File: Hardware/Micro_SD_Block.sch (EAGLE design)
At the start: 14 parts, among them U1 USD-SOCKETNEW, U2 EDISON_CONNECTOR_FULLMOUNTING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, U3 EDISON_CONNECTOR_FULLHEADER

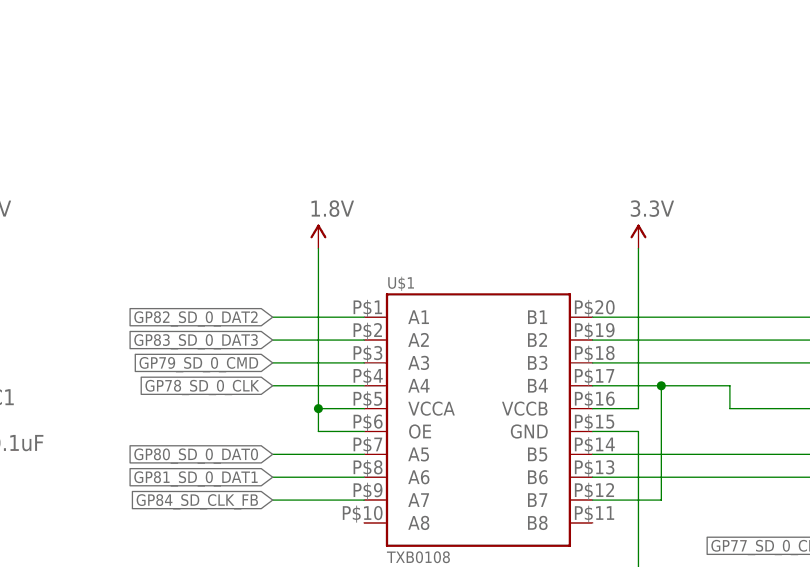
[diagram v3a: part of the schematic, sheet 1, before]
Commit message: Ready for reds Struck one weird leftover via Renamed TXB0108 chip refdes To-do: fix the TXB0108 symbol to remove P$ from pin names. Do in library and update to design!
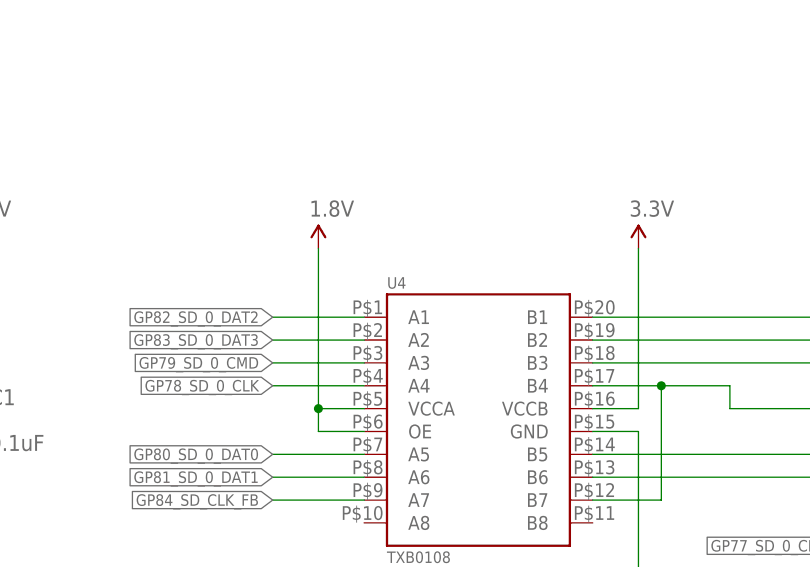
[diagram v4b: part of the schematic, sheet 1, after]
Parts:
- renumbered U$1 to U4
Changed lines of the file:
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@@
 <layer number="255" name="routoute" color="7" fill="1" visible="yes" active="yes"/>
 </layers>
-<schematic xreflabel="%F%N/%S" xrefpart="1_/%S.%C%R">
+<schematic xreflabel="%F%N/%S" xrefpart="/%S.%C%R">
 <attributes>
 </attributes>
@@
 <part name="FID3" library="SparkFun-Aesthetics" deviceset="FIDUCIAL" device="1X2"/>
 <part name="FID4" library="SparkFun-Aesthetics" deviceset="FIDUCIAL" device="1X2"/>
-<part name="U$1" library="Testing" deviceset="TXB0108" device=""/>
+<part name="U4" library="Testing" deviceset="TXB0108" device=""/>
 <part name="GND2" library="SparkFun-Aesthetics" deviceset="GND" device=""/>
 <part name="SUPPLY1" library="SparkFun-Aesthetics" deviceset="3.3V" device=""/>
@@
 <instance part="FID3" gate="G$1" x="246.38" y="30.48"/>
 <instance part="FID4" gate="G$1" x="241.3" y="30.48"/>
-<instance part="U$1" gate="G$1" x="121.92" y="109.22"/>
+<instance part="U4" gate="G$1" x="121.92" y="109.22"/>
 <instance part="GND2" gate="1" x="132.08" y="83.82"/>
 <instance part="SUPPLY1" gate="G$1" x="132.08" y="127"/>
@@
 </segment>
 <segment>
-<pinref part="U$1" gate="G$1" pin="GND"/>
+<pinref part="U4" gate="G$1" pin="GND"/>
 <wire x1="127" y1="106.68" x2="132.08" y2="106.68" width="0.1524" layer="91"/>
 <wire x1="132.08" y1="106.68" x2="132.08" y2="86.36" width="0.1524" layer="91"/>
@@
 <wire x1="101.6" y1="111.76" x2="91.44" y2="111.76" width="0.1524" layer="91"/>
 <label x="91.44" y="111.76" size="1.27" layer="95" rot="R180" xref="yes"/>
-<pinref part="U$1" gate="G$1" pin="A4"/>
+<pinref part="U4" gate="G$1" pin="A4"/>
 </segment>
 </net>
@@
 <wire x1="101.6" y1="114.3" x2="91.44" y2="114.3" width="0.1524" layer="91"/>
 <label x="91.44" y="114.3" size="1.27" layer="95" rot="R180" xref="yes"/>
-<pinref part="U$1" gate="G$1" pin="A3"/>
+<pinref part="U4" gate="G$1" pin="A3"/>
 </segment>
 </net>
@@
 <wire x1="101.6" y1="104.14" x2="91.44" y2="104.14" width="0.1524" layer="91"/>
 <label x="91.44" y="104.14" size="1.27" layer="95" rot="R180" xref="yes"/>
-<pinref part="U$1" gate="G$1" pin="A5"/>
+<pinref part="U4" gate="G$1" pin="A5"/>
 </segment>
 </net>
@@
 <wire x1="101.6" y1="101.6" x2="91.44" y2="101.6" width="0.1524" layer="91"/>
 <label x="91.44" y="101.6" size="1.27" layer="95" rot="R180" xref="yes"/>
-<pinref part="U$1" gate="G$1" pin="A6"/>
+<pinref part="U4" gate="G$1" pin="A6"/>
 </segment>
 </net>
@@
 <wire x1="101.6" y1="119.38" x2="91.44" y2="119.38" width="0.1524" layer="91"/>
 <label x="91.44" y="119.38" size="1.27" layer="95" rot="R180" xref="yes"/>
-<pinref part="U$1" gate="G$1" pin="A1"/>
+<pinref part="U4" gate="G$1" pin="A1"/>
 </segment>
 </net>
@@
 <wire x1="101.6" y1="116.84" x2="91.44" y2="116.84" width="0.1524" layer="91"/>
 <label x="91.44" y="116.84" size="1.27" layer="95" rot="R180" xref="yes"/>
-<pinref part="U$1" gate="G$1" pin="A2"/>
+<pinref part="U4" gate="G$1" pin="A2"/>
 </segment>
 </net>
 <net name="N$1" class="0">
 <segment>
-<pinref part="U$1" gate="G$1" pin="B1"/>
+<pinref part="U4" gate="G$1" pin="B1"/>
 <pinref part="U1" gate="G$1" pin="NC"/>
 <wire x1="127" y1="119.38" x2="162.56" y2="119.38" width="0.1524" layer="91"/>
@@
 <segment>
 <pinref part="U1" gate="G$1" pin="CS"/>
-<pinref part="U$1" gate="G$1" pin="B2"/>
+<pinref part="U4" gate="G$1" pin="B2"/>
 <wire x1="162.56" y1="116.84" x2="127" y2="116.84" width="0.1524" layer="91"/>
 </segment>
@@
 <net name="N$3" class="0">
 <segment>
-<pinref part="U$1" gate="G$1" pin="B3"/>
+<pinref part="U4" gate="G$1" pin="B3"/>
 <pinref part="U1" gate="G$1" pin="DI"/>
 <wire x1="127" y1="114.3" x2="162.56" y2="114.3" width="0.1524" layer="91"/>
@@
 <net name="SCK" class="0">
 <segment>
-<pinref part="U$1" gate="G$1" pin="B4"/>
+<pinref part="U4" gate="G$1" pin="B4"/>
 <wire x1="127" y1="111.76" x2="134.62" y2="111.76" width="0.1524" layer="91"/>
 <wire x1="134.62" y1="111.76" x2="142.24" y2="111.76" width="0.1524" layer="91"/>
@@
 <pinref part="U1" gate="G$1" pin="SCK"/>
 <wire x1="142.24" y1="109.22" x2="162.56" y2="109.22" width="0.1524" layer="91"/>
-<pinref part="U$1" gate="G$1" pin="B7"/>
+<pinref part="U4" gate="G$1" pin="B7"/>
 <wire x1="127" y1="99.06" x2="134.62" y2="99.06" width="0.1524" layer="91"/>
 <wire x1="134.62" y1="99.06" x2="134.62" y2="111.76" width="0.1524" layer="91"/>
@@
 <net name="N$5" class="0">
 <segment>
-<pinref part="U$1" gate="G$1" pin="B5"/>
+<pinref part="U4" gate="G$1" pin="B5"/>
 <pinref part="U1" gate="G$1" pin="DO"/>
 <wire x1="127" y1="104.14" x2="162.56" y2="104.14" width="0.1524" layer="91"/>
@@
 <net name="N$6" class="0">
 <segment>
-<pinref part="U$1" gate="G$1" pin="B6"/>
+<pinref part="U4" gate="G$1" pin="B6"/>
 <pinref part="U1" gate="G$1" pin="RSV"/>
 <wire x1="127" y1="101.6" x2="162.56" y2="101.6" width="0.1524" layer="91"/>
@@
 <net name="3.3V" class="0">
 <segment>
-<pinref part="U$1" gate="G$1" pin="VCCB"/>
+<pinref part="U4" gate="G$1" pin="VCCB"/>
 <wire x1="127" y1="109.22" x2="132.08" y2="109.22" width="0.1524" layer="91"/>
 <wire x1="132.08" y1="109.22" x2="132.08" y2="127" width="0.1524" layer="91"/>
@@
 <net name="1.8V" class="0">
 <segment>
-<pinref part="U$1" gate="G$1" pin="VCCA"/>
+<pinref part="U4" gate="G$1" pin="VCCA"/>
 <pinref part="SUPPLY3" gate="G$1" pin="1.8V"/>
 <wire x1="101.6" y1="109.22" x2="96.52" y2="109.22" width="0.1524" layer="91"/>
 <wire x1="96.52" y1="109.22" x2="96.52" y2="127" width="0.1524" layer="91"/>
-<pinref part="U$1" gate="G$1" pin="OE"/>
+<pinref part="U4" gate="G$1" pin="OE"/>
 <wire x1="101.6" y1="106.68" x2="96.52" y2="106.68" width="0.1524" layer="91"/>
 <wire x1="96.52" y1="106.68" x2="96.52" y2="109.22" width="0.1524" layer="91"/>
@@
 <wire x1="101.6" y1="99.06" x2="91.44" y2="99.06" width="0.1524" layer="91"/>
 <label x="91.44" y="99.06" size="1.27" layer="95" rot="R180" xref="yes"/>
-<pinref part="U$1" gate="G$1" pin="A7"/>
-</segment>
-</net>
+<pinref part="U4" gate="G$1" pin="A7"/>
+</segment>
+</net>

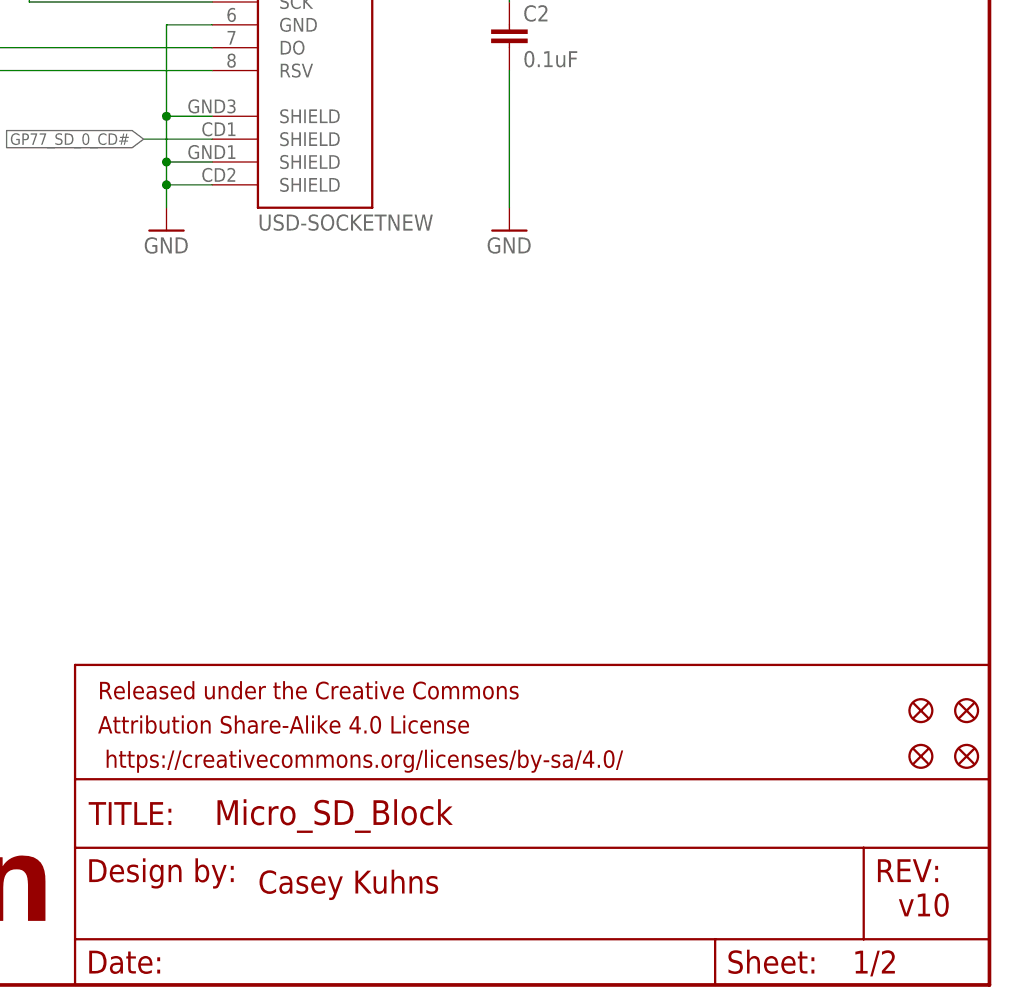
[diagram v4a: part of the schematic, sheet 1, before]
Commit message: fixed CD grounding issue, CD1 and CD2 are connected internally.
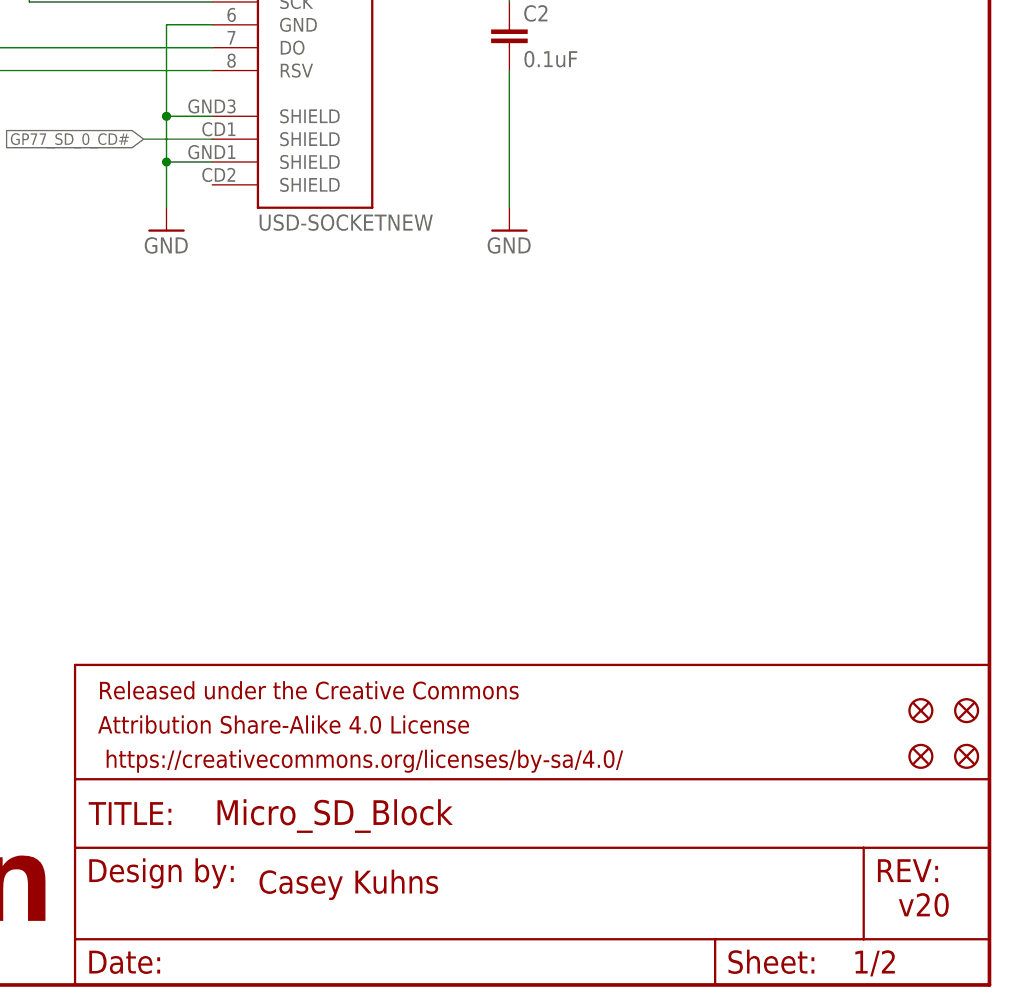
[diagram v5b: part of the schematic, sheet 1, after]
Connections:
- net GND: no longer U1.SHIELD@4
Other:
- note added: "v20"
- note removed: "v10"
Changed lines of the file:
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@@
 <?xml version="1.0" encoding="utf-8"?>
 <!DOCTYPE eagle SYSTEM "eagle.dtd">
-<eagle version="6.6.0">
+<eagle version="6.5.0">
 <drawing>
 <settings>
@@
 <plain>
 <text x="167.64" y="10.16" size="2.54" layer="94">Casey Kuhns</text>
-<text x="238.76" y="7.62" size="2.54" layer="94">v10</text>
+<text x="238.76" y="7.62" size="2.54" layer="94">v20</text>
 </plain>
 <instances>
@@
 <pinref part="U1" gate="G$1" pin="SHIELD@1"/>
 <wire x1="162.56" y1="96.52" x2="157.48" y2="96.52" width="0.1524" layer="91"/>
-<pinref part="U1" gate="G$1" pin="SHIELD@4"/>
 <wire x1="157.48" y1="96.52" x2="157.48" y2="91.44" width="0.1524" layer="91"/>
-<wire x1="157.48" y1="91.44" x2="157.48" y2="88.9" width="0.1524" layer="91"/>
-<wire x1="157.48" y1="88.9" x2="162.56" y2="88.9" width="0.1524" layer="91"/>
 <pinref part="U1" gate="G$1" pin="SHIELD@3"/>
 <wire x1="162.56" y1="91.44" x2="157.48" y2="91.44" width="0.1524" layer="91"/>
 <junction x="157.48" y="91.44"/>
 <pinref part="GND1" gate="1" pin="GND"/>
-<wire x1="157.48" y1="86.36" x2="157.48" y2="88.9" width="0.1524" layer="91"/>
-<junction x="157.48" y="88.9"/>
+<wire x1="157.48" y1="86.36" x2="157.48" y2="91.44" width="0.1524" layer="91"/>
 <pinref part="U1" gate="G$1" pin="GND"/>
 <wire x1="162.56" y1="106.68" x2="157.48" y2="106.68" width="0.1524" layer="91"/>
